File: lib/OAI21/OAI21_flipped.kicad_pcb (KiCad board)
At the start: 2 copper layers, 6 parts

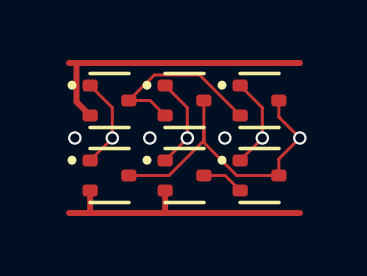
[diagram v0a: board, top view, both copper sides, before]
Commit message: High-density layout with pitch of 1.1mm, which gains 23% !!
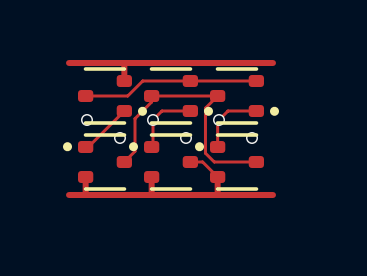
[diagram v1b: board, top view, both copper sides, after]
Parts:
- moved P3 0.87 mm to (5.50, 3.30)
- moved N3 0.76 mm to (5.50, 1.10), turned to 180 degrees
- moved P2 0.64 mm to (3.30, 3.30)
- moved N2 0.47 mm to (3.30, 1.10), turned to 180 degrees
- moved P1 0.47 mm to (1.10, 3.30)
- moved N1 0.21 mm to (1.10, 1.10), turned to 180 degrees
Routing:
- net GND: track 9.64 -> 7.42 mm
- net Y: track 10.9 -> 8.67 mm, vias 1 -> 0
- net A: track 3.11 -> 2.03 mm
- net B2: track 3.11 -> 2.29 mm
- net B1: track 3.11 -> 2.29 mm
- net intB: track 1.42 -> 0.87 mm
- net VDD: track 9.20 -> 8.66 mm

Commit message: All cells now use 1mm*4mm grid rather than 1.1mm*4.4mm
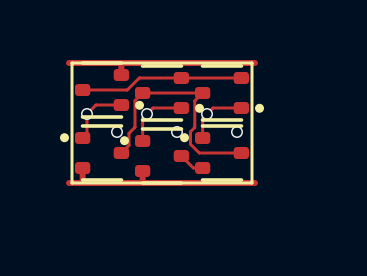
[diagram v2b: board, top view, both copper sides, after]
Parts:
- moved P3 0.58 mm to (5.00, 3.00)
- moved N3 0.51 mm to (5.00, 1.00)
- moved P2 0.36 mm to (3.00, 3.10)
- moved N2 0.32 mm to (3.00, 1.00)
- moved P1 0.32 mm to (1.00, 3.00)
- moved N1 0.22 mm to (1.00, 0.90)
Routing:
- net VDD: track 8.66 -> 7.14 mm
- net GND: track 7.42 -> 6.62 mm
- net Y: track 8.67 -> 7.99 mm

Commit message: Make the pads of my SOT523 footprint very slightly smaller, which is enough to route all the cells and leave the mosfets exactly on the grid
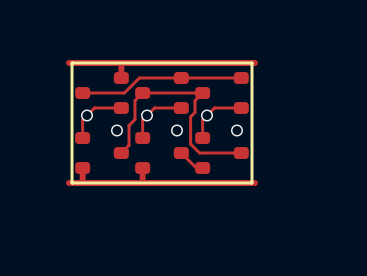
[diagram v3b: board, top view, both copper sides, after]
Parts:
- N1, N2, N3, P1, P2, P3: footprint Package_TO_SOT_SMD:SOT-523 -> RV523:SOT523
- moved P2 0.10 mm to (3.00, 3.00)
- moved N1 0.10 mm to (1.00, 1.00)

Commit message: Propagate MOSFET values to the cells' PCBs
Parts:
- N1, N2, N3: value (none) -> NMOS
- P1, P2, P3: value (none) -> PMOS
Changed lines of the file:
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@@
 			)
 		)
-		(property "Value" ""
+		(property "Value" "PMOS"
 			(at 0 0 0)
 			(layer "F.Fab")
@@
 			)
 		)
-		(property "Value" ""
+		(property "Value" "NMOS"
 			(at 0 0 180)
 			(layer "F.Fab")
@@
 			)
 		)
-		(property "Value" ""
+		(property "Value" "NMOS"
 			(at 0 0 180)
 			(layer "F.Fab")
@@
 			)
 		)
-		(property "Value" ""
+		(property "Value" "PMOS"
 			(at 0 0 0)
 			(layer "F.Fab")
@@
 			)
 		)
-		(property "Value" ""
+		(property "Value" "NMOS"
 			(at 0 0 180)
 			(layer "F.Fab")
@@
 			)
 		)
-		(property "Value" ""
+		(property "Value" "PMOS"
 			(at 0 0 0)
 			(layer "F.Fab")

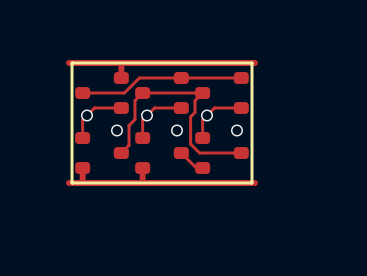
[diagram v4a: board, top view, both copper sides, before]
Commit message: Pad Y of OAI21 flipped was not properly connected
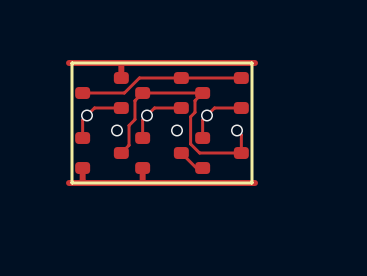
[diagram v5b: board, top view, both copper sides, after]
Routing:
- net Y: track 7.98 -> 8.79 mm, vias 0 -> 1
- net (no net): vias 3 -> 2
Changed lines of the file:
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@@
-	)
-	(via
-		(at 5.5 2.25)
-		(size 0.4)
-		(drill 0.3)
-		(layers "F.Cu" "B.Cu")
-		(net 0)
 	)
 	(via
@@
 	)
 	(segment
+		(start 5.645 3)
+		(end 5.645 2.395)
+		(width 0.1)
+		(layer "F.Cu")
+		(net 2)
+	)
+	(segment
 		(start 4.253188 3)
 		(end 3.954 2.700812)
@@
 		(start 5.645 3)
 		(end 4.253188 3)
+		(width 0.1)
+		(layer "F.Cu")
+		(net 2)
+	)
+	(segment
+		(start 5.645 2.395)
+		(end 5.5 2.25)
 		(width 0.1)
 		(layer "F.Cu")
@@
 		(net 2)
 	)
+	(via
+		(at 5.5 2.25)
+		(size 0.4)
+		(drill 0.3)
+		(layers "F.Cu" "B.Cu")
+		(net 2)
+	)
